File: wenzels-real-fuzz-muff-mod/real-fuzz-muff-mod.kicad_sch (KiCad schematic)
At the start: 101 parts, among them J1 Input jack, J2 Output jack, J3 18V, Q1 J113, Q2 J113, Q3 J113, Q4 J113, T1 2n2369a, T2 2n2369a, T3 2n2369a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

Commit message: wenzels-real-fuzz-muff-mod: r2-wip-1
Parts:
- added C33, C34, C35, C36: 10u, symbol Device:C_Polarized
- added D10, D7: BLUE, symbol Device:LED
- added D8, D9: ORANGE, symbol Device:LED
- added SW1: CLIP1-P, Button_Switch_SMD:Nidec_Copal_CAS-120A, symbol Switch:SW_Nidec_CAS-120A1
- added SW2: CLIP1-N, Button_Switch_SMD:Nidec_Copal_CAS-120A, symbol Switch:SW_Nidec_CAS-120A1
- added SW3: CLIP2-P, Button_Switch_SMD:Nidec_Copal_CAS-120A, symbol Switch:SW_Nidec_CAS-120A1
- added SW4: CLIP2-N, Button_Switch_SMD:Nidec_Copal_CAS-120A, symbol Switch:SW_Nidec_CAS-120A1
- VOLTS1, VOLTS2: value B1M -> A1M
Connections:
- net GND: now also C33.2, C34.2, C35.2, C36.2
- net at D1.2 (A), D2.1 (K): no longer C5.2
- net at C10.1, C9.2, R14.2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: now also C8.1
- net at D3.2 (A), D4.1 (K): no longer C8.2
- net at R16.1, T3.1 (E): now also C35.1
- net at C9.1, R12.2, R13.1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: now also D10.1 (K), D9.2 (A)
- net at C6.1, R7.2, R8.1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: now also D7.2 (A), D8.1 (K)
- net at R22.1, T4.1 (E): now also C36.1
- net at R11.1, T2.1 (E): now also C34.1
- net at C6.2, C7.1, R10.2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: now also C5.1
- net at R5.1, T1.1 (E): now also C33.1
- new net: D9.1 (K), SW3.2 (B), SW3.3 (A)
- new net: C5.2, SW1.1 (C), SW2.1 (C)
- new net: D7.1 (K), SW1.2 (B), SW1.3 (A)
- new net: C8.2, SW3.1 (C), SW4.1 (C)
- new net: D10.2 (A), SW4.2 (B), SW4.3 (A)
- new net: D8.2 (A), SW2.2 (B), SW2.3 (A)
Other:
- note added: "Don’t solder D1 & D2 (or cut them off)."
- note added: "LEDs forward voltage measurements RED - 1.93V GREEN - 2.02V BLUE - 2.63V ORANGE - 1.97V YELLOW - 2.10V WHITE - 2.73V"
- note removed: "Just do not put D1, D2, and C5 onto the PCB. Or unsolder C5 if they are already there."
- note removed: "Just do not put D3, D4, and C8 onto the PCB. Or unsolder C8 if they are already there."
- note removed: "Known issues to be addressed in a future revision: 1. Not enough gain, even with T1 and T4 in series the clipping stages are barely clipping at maxed out GAIN. Without clipping diodes they need much more juice to really go high gain. Something like SD-1 pedal in front can give it a proper push. 2. VOLTS knobs have very tiny and sensitive range where you really voltage-starve the transistors, it’s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"
- moved on the sheet: C14, C5, C8, D1, D2, D3, D4

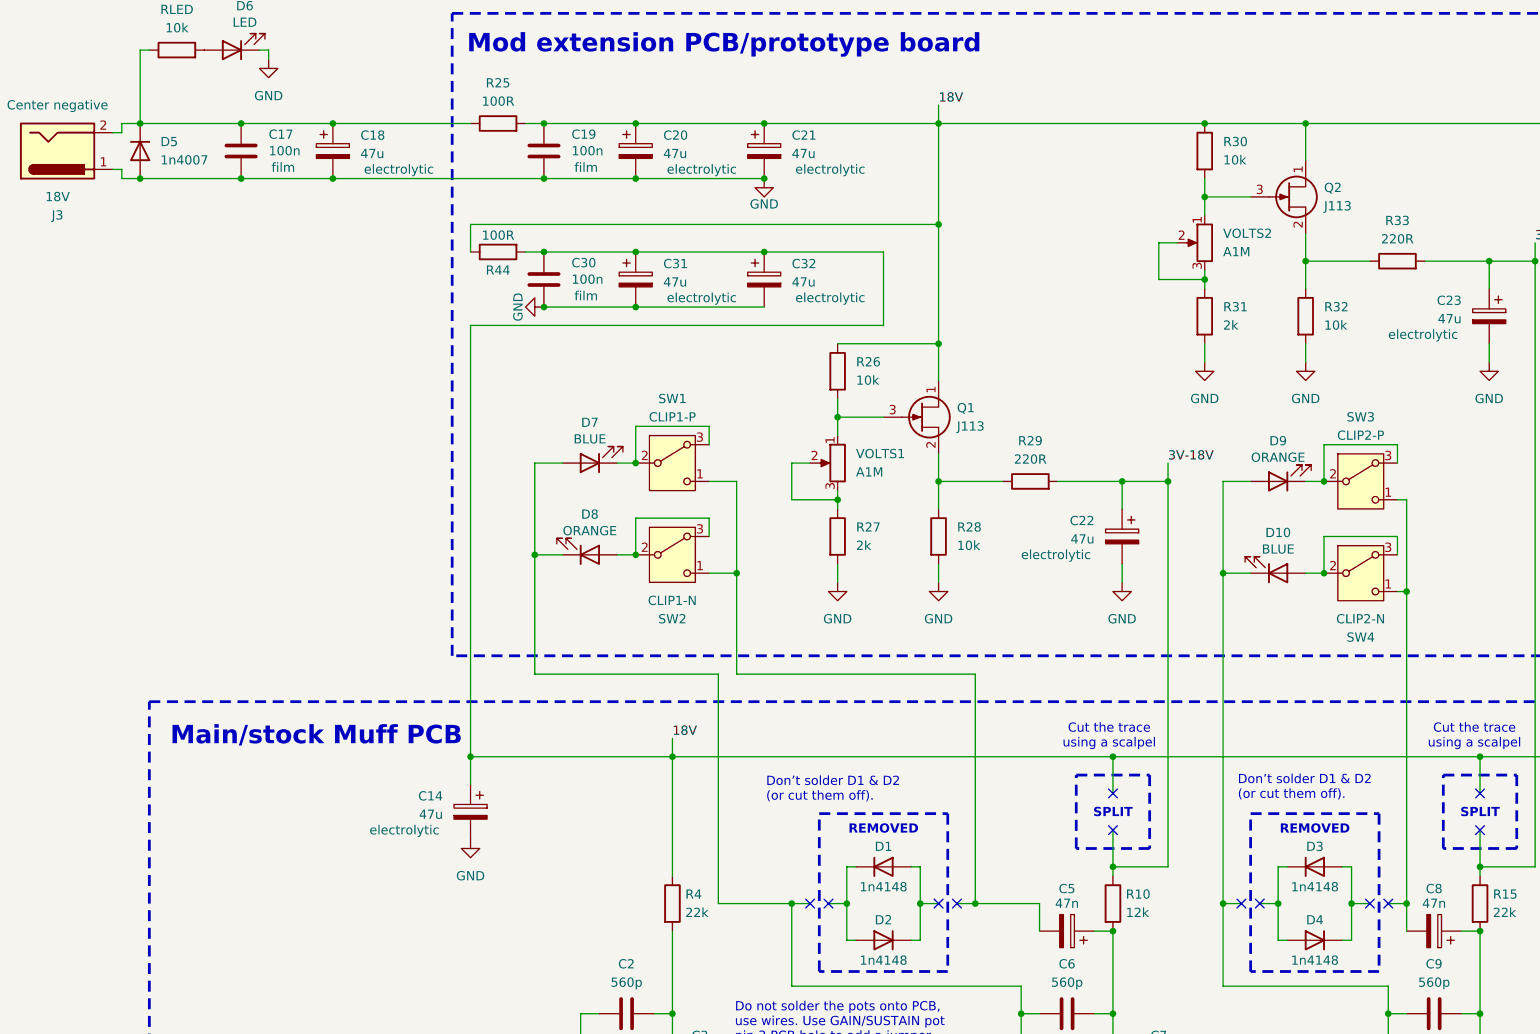
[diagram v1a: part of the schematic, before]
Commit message: wenzels-real-fuzz-muff-mod release-2026-03-r2
Maximized gain, switchable optional LED clipping diodes, logarithmic
VOLTS pots.
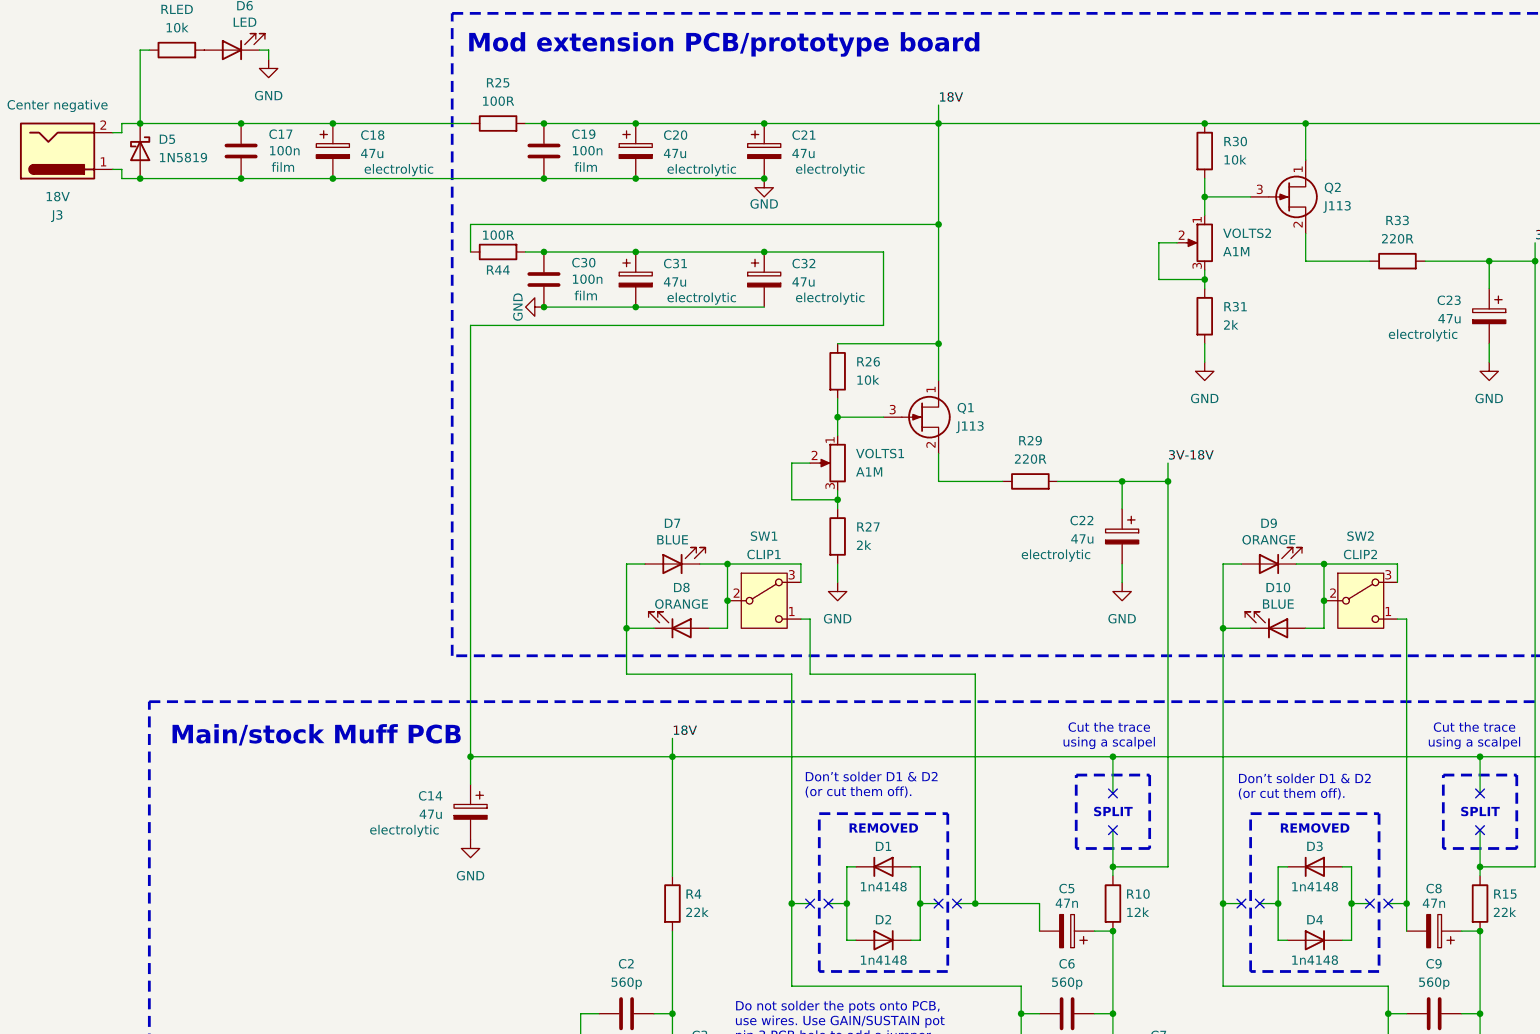
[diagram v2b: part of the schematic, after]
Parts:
- removed D5: 1n4007, symbol Device:D
- removed R28, R32: 10k, symbol Device:R
- removed SW2: CLIP1-N, Button_Switch_SMD:Nidec_Copal_CAS-120A, symbol Switch:SW_Nidec_CAS-120A1
- removed SW4: CLIP2-N, Button_Switch_SMD:Nidec_Copal_CAS-120A, symbol Switch:SW_Nidec_CAS-120A1
- added D5: 1N5819, Diode_THT:D_DO-41_SOD81_P10.16mm_Horizontal, symbol Diode:1N5819
- SW1: value CLIP1-P -> CLIP1
- SW2: renamed from SW3; value CLIP2-P -> CLIP2
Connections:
- net GND: now also D5.2 (A)
- net at D9.1 (K), SW2.2 (B), SW2.3 (A): now also D10.2 (A)
- net at D7.1 (K), SW1.2 (B), SW1.3 (A): now also D8.2 (A)
- net at C17.1, C18.1, J3.2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: now also D5.1 (K)
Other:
- moved on the sheet: D10, D7, D8, D9, SW1, SW2
